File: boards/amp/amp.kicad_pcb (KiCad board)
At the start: 2 copper layers, 156.8 x 184.6 mm, 24 parts, among them J10 CONN_01X02, J11 CONN_01X02, J12 CONN_01X02, U18 APA102C_x5, U21 APA102C_x7, U23 APA102C_x7, U24 APA102C_x3, U26 APA102C_x7, U27 APA102C_x2, U28 APA102C_x3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

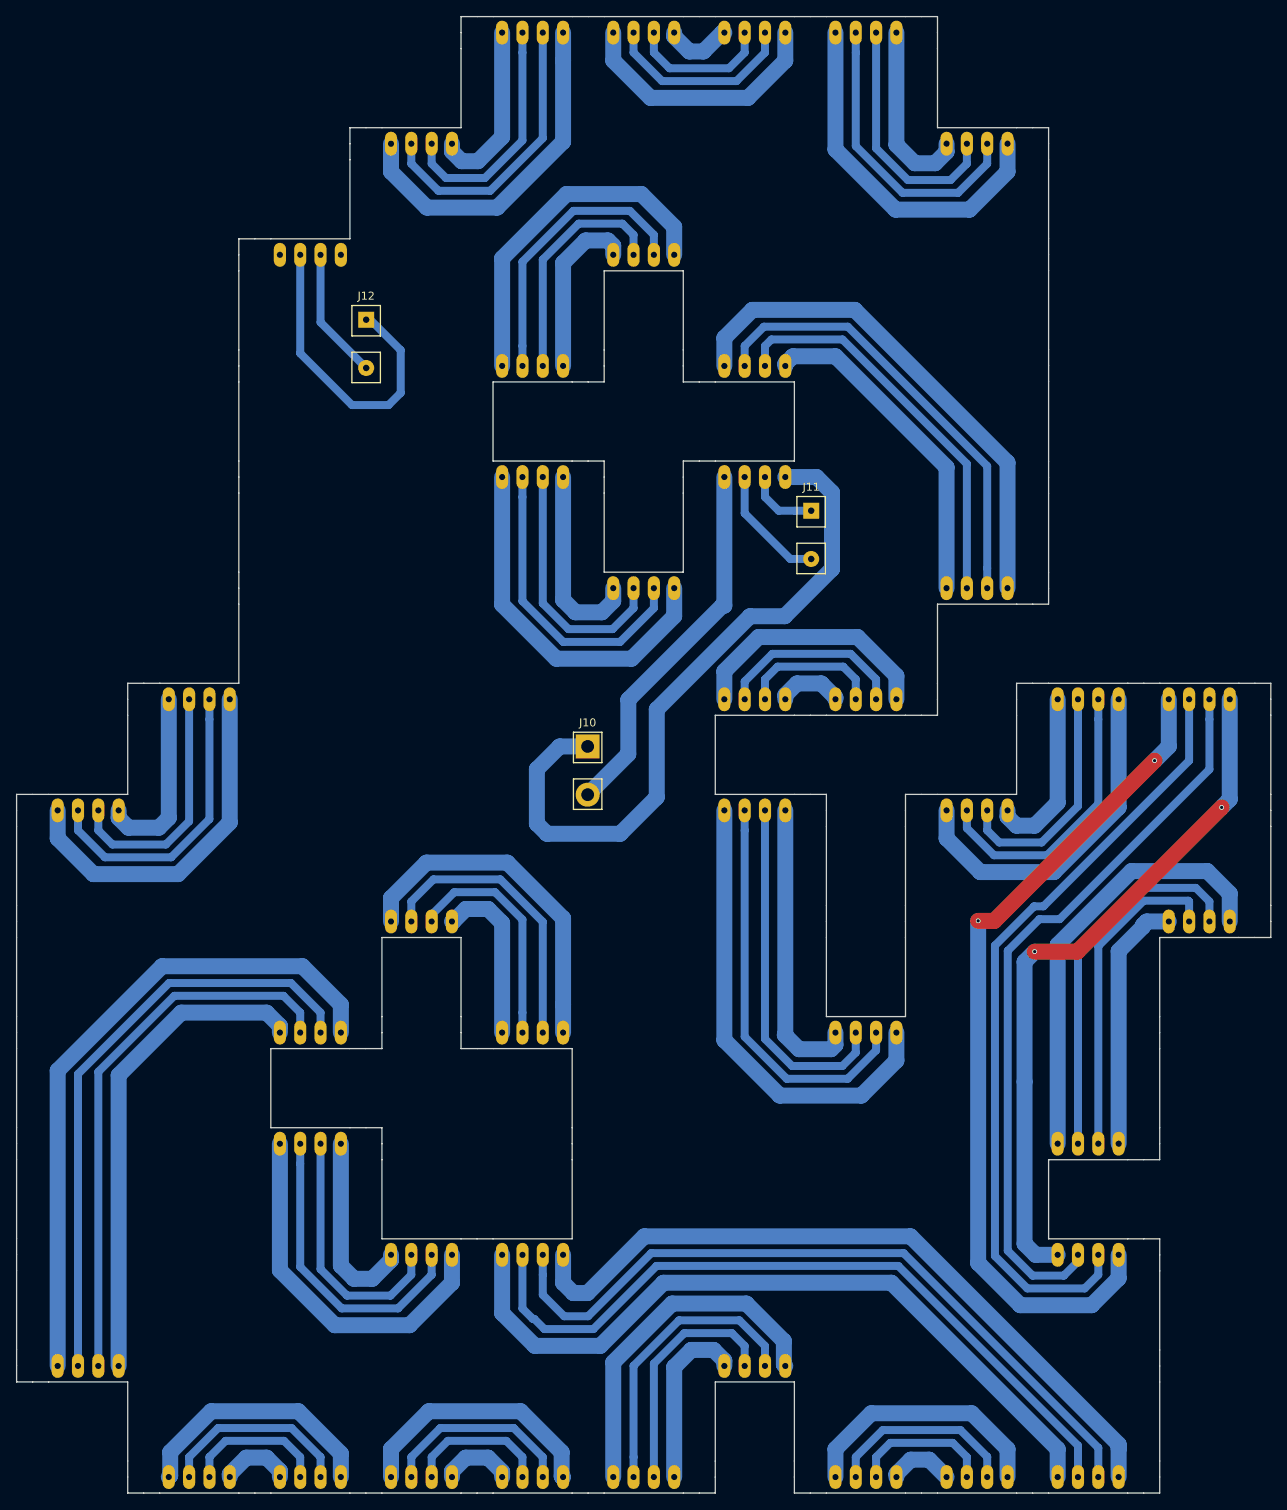
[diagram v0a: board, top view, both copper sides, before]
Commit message: Generate gerbers for all letters. Use a single drill size.
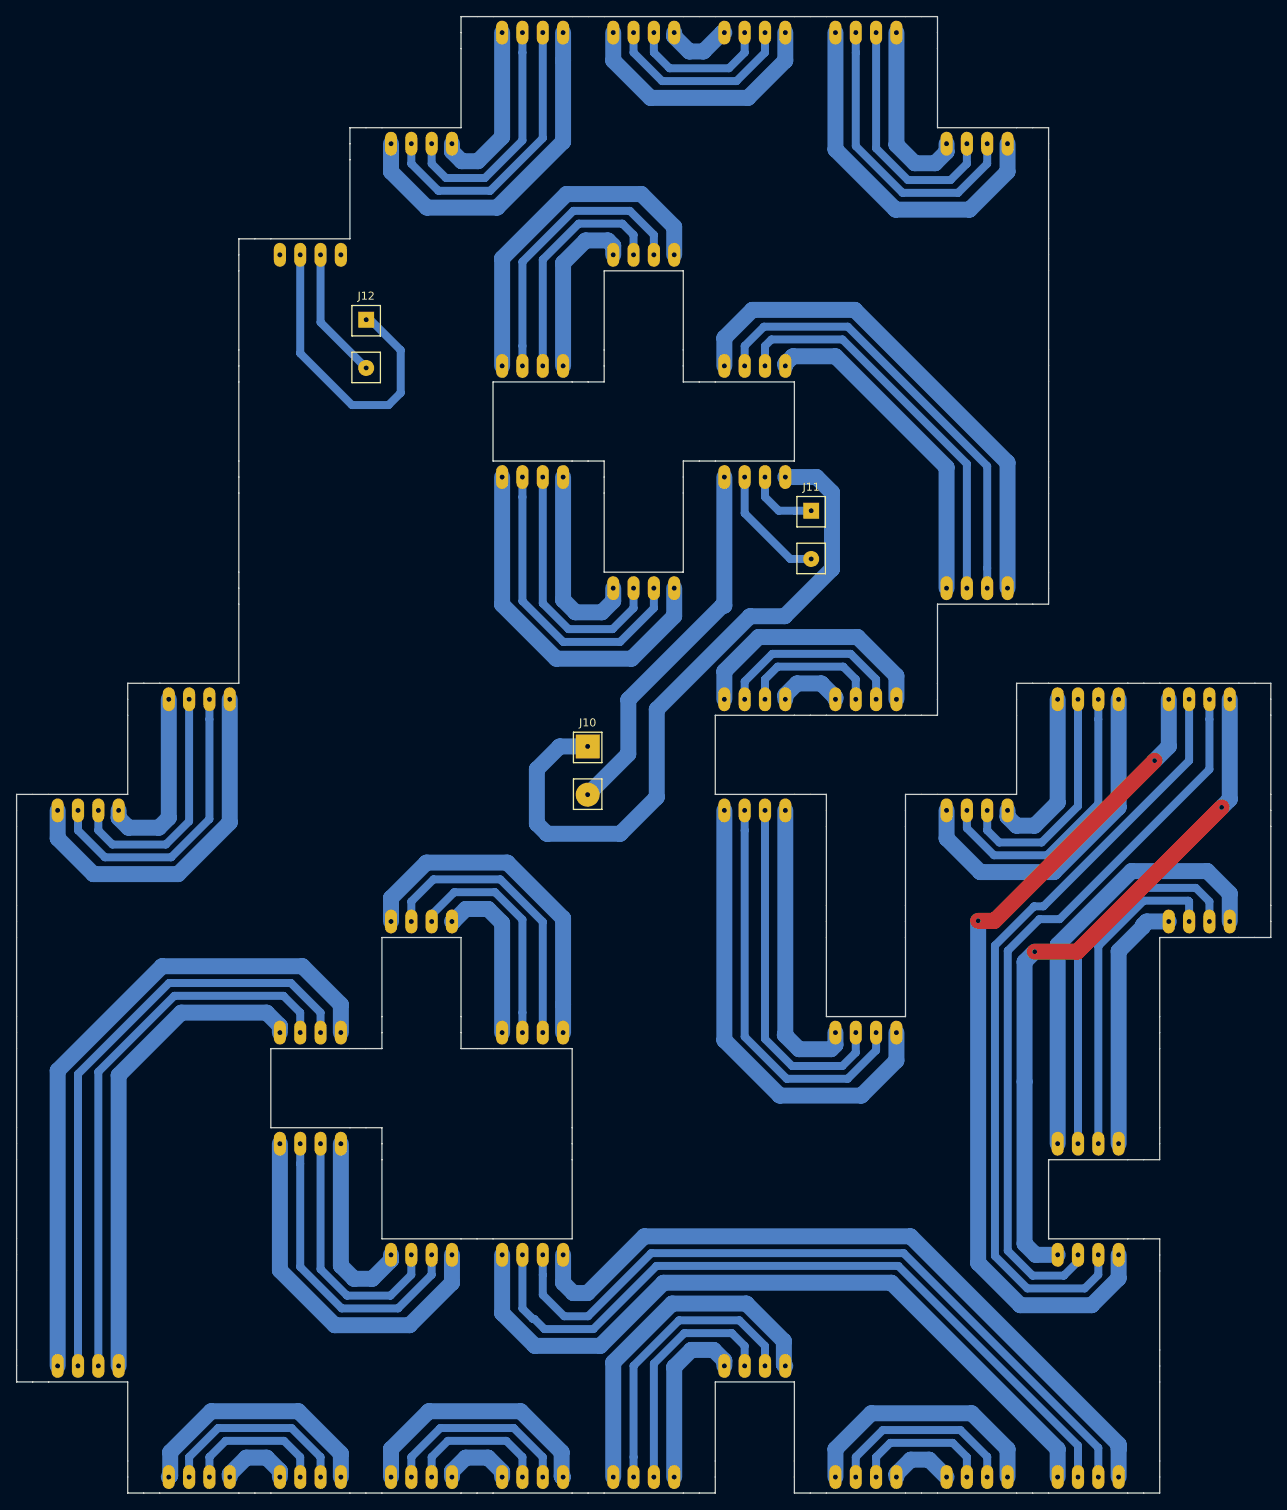
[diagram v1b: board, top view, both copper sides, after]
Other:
- net class Default: via_dia 0.6 -> 1; via_drill 0.4 -> 0.6
- net class Signal: via_dia 0.6 -> 1; via_drill 0.4 -> 0.6
